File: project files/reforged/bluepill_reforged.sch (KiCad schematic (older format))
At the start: 41 parts, among them J1 USB_C_Receptacle_USB2.0, J2 Left Castellation, J3 STDC14, J4 Right Castellation, J5 STDC14, SW1 Boot0, SW2 Reset, U1 AMS1117-3.3, U2 STM32F103C8Tx, Y1 8MHz, Y2 MC-306, 32768Hz

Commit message: Updates after re-opening in KiCAD 5.1.7
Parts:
- J1: symbol Connector:USB_C_Receptacle_USB2.0 -> bluepill_reforged-rescue:USB_C_Receptacle_USB2.0-Connector
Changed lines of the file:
@@
 Other effective low-drop linear regulators are:\nTI LM3940, up to 1A, but isincompatible in pinout\nLMS8117AMP3.3\n
 $Comp
-L Connector:USB_C_Receptacle_USB2.0 J1
+L bluepill_reforged-rescue:USB_C_Receptacle_USB2.0-Connector J1
 U 1 1 5E12D596
 P 1000 1650

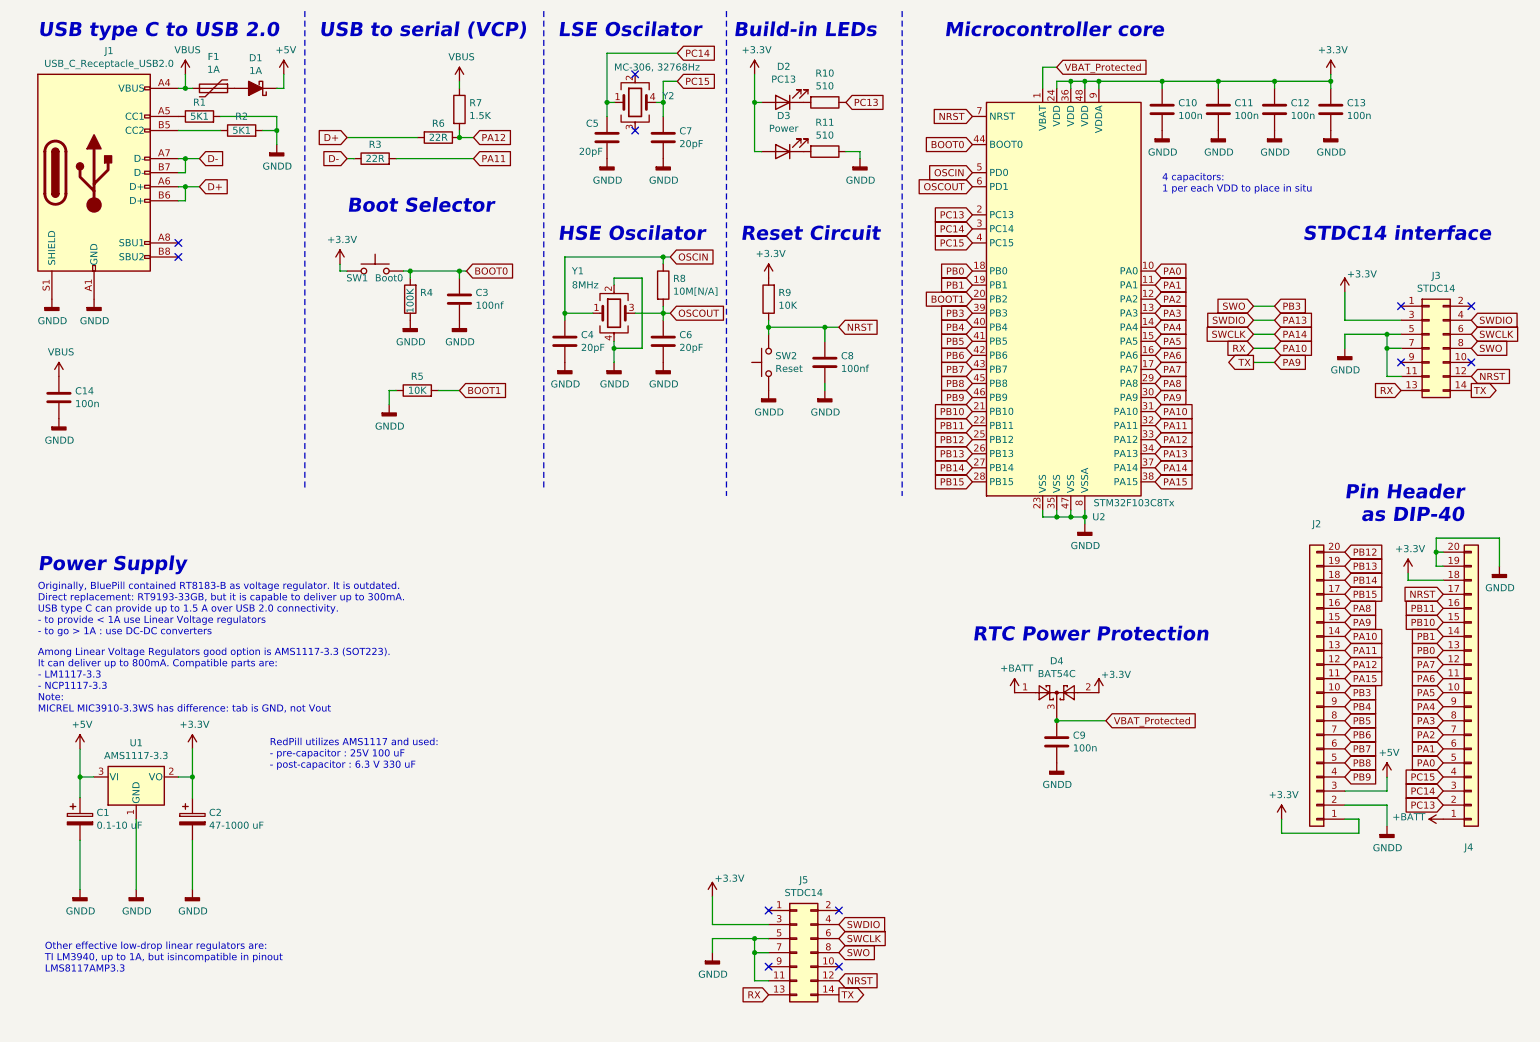
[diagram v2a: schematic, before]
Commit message: Replaced the symbol of STDC14
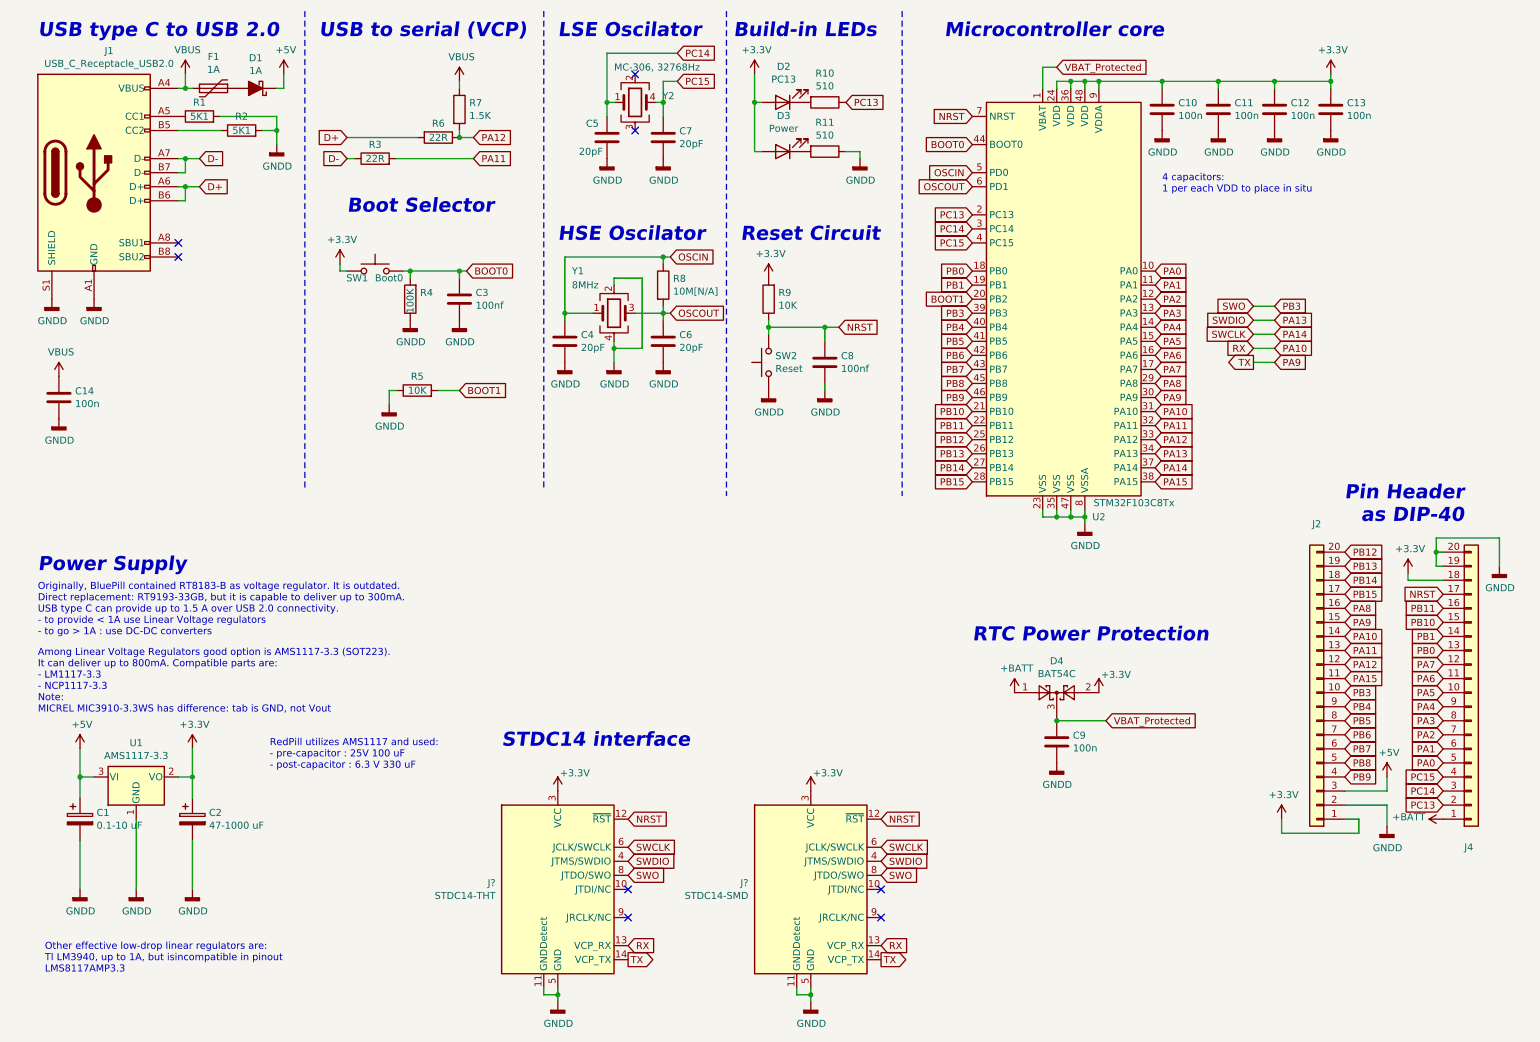
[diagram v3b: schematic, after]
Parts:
- removed J3: STDC14, Connector_PinHeader_1.27mm:PinHeader_2x07_P1.27mm_Vertical_SMD, symbol Connector_Generic:Conn_02x07_Odd_Even
- removed J5: STDC14, Connector_PinHeader_1.27mm:PinHeader_2x07_P1.27mm_Vertical, symbol Connector_Generic:Conn_02x07_Odd_Even
- added J?: STDC14-SMD, symbol Connector:Conn_ST_STDC14
- added J?: STDC14-THT, symbol Connector:Conn_ST_STDC14
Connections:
- net +3V3: now also J?.3 (VCC), J?.3 (VCC)
- net GNDD: now also J?.11 (GNDDetect), J?.11 (GNDDetect), J?.5 (GND), J?.5 (GND), J?.7 (GND), J?.7 (GND)
- net NRST: now also J?.12 (~RST), J?.12 (~RST)
- net PA10: now also J?.13 (VCP_RX), J?.13 (VCP_RX)
- net PA13: now also J?.4 (JTMS/SWDIO), J?.4 (JTMS/SWDIO)
- net PA14: now also J?.6 (JCLK/SWCLK), J?.6 (JCLK/SWCLK)
- net PA9: now also J?.14 (VCP_TX), J?.14 (VCP_TX)
- net PB3: now also J?.8 (JTDO/SWO), J?.8 (JTDO/SWO)
- no-connect marks 12 -> 8
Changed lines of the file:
@@
 Text GLabel 9400 2600 2    50   Input ~ 0
 PB3
-Text Notes 9600 2150 0    100  Italic 20
+Text Notes 3900 5750 0    100  Italic 20
 STDC14 interface
 $Comp
@@
 $EndComp
 Connection ~ 7850 5550
-$Comp
-L Connector_Generic:Conn_02x07_Odd_Even J3
-U 1 1 5E19328C
-P 10500 2900
-F 0 "J3" H 10550 3417 50  0000 C CNN
-F 1 "STDC14" H 10550 3326 50  0000 C CNN
-F 2 "Connector_PinHeader_1.27mm:PinHeader_2x07_P1.27mm_Vertical_SMD" H 10500 2900 50  0001 C CNN
-F 3 "~" H 10500 2900 50  0001 C CNN
-	1    10500 2900
-	1    0    0    -1
-$EndComp
-NoConn ~ 10300 2600
-NoConn ~ 10800 2600
-Text GLabel 10800 2800 2    50   Input ~ 0
-SWCLK
-Text GLabel 10800 3100 2    50   Input ~ 0
-NRST
-Text GLabel 10800 2700 2    50   Input ~ 0
-SWDIO
-$Comp
-L power:+3.3V #PWR037
-U 1 1 5E1A21E5
-P 9900 2500
-F 0 "#PWR037" H 9900 2350 50  0001 C CNN
-F 1 "+3.3V" H 9915 2628 50  0000 L CNN
-F 2 "" H 9900 2500 50  0001 C CNN
-F 3 "" H 9900 2500 50  0001 C CNN
-	1    9900 2500
-	1    0    0    -1
-$EndComp
-Wire Wire Line
-	10300 2700 9900 2700
-Wire Wire Line
-	9900 2700 9900 2500
-Text GLabel 10800 2900 2    50   Input ~ 0
-SWO
-NoConn ~ 10800 3000
-NoConn ~ 10300 3000
-Wire Wire Line
-	10300 2800 10200 2800
-Wire Wire Line
-	10200 2800 10200 2900
-Wire Wire Line
-	10200 2900 10300 2900
-Wire Wire Line
-	10300 3100 10200 3100
-Wire Wire Line
-	10200 3100 10200 2900
-Connection ~ 10200 2900
-Wire Wire Line
-	10200 2800 9900 2800
-Wire Wire Line
-	9900 2800 9900 2900
-Connection ~ 10200 2800
-Text GLabel 10800 3200 2    50   Output ~ 0
-TX
-Text GLabel 10300 3200 0    50   Input ~ 0
-RX
 Text GLabel 9250 2900 0    50   Input ~ 0
 RX
@@
 $EndComp
 $Comp
-L power:GNDD #PWR0117
-U 1 1 5E9096B4
-P 9900 2900
-F 0 "#PWR0117" H 9900 2650 50  0001 C CNN
-F 1 "GNDD" H 9904 2745 50  0000 C CNN
-F 2 "" H 9900 2900 50  0001 C CNN
-F 3 "" H 9900 2900 50  0001 C CNN
-	1    9900 2900
-	1    0    0    -1
-$EndComp
-$Comp
 L power:GNDD #PWR0118
 U 1 1 5E909F75
@@
 Wire Wire Line
 	10200 6150 10200 6300
-$Comp
-L Connector_Generic:Conn_02x07_Odd_Even J5
-U 1 1 5F2A0D58
-P 6000 7200
-F 0 "J5" H 6050 7717 50  0000 C CNN
-F 1 "STDC14" H 6050 7626 50  0000 C CNN
-F 2 "Connector_PinHeader_1.27mm:PinHeader_2x07_P1.27mm_Vertical" H 6000 7200 50  0001 C CNN
-F 3 "~" H 6000 7200 50  0001 C CNN
-	1    6000 7200
-	1    0    0    -1
-$EndComp
-NoConn ~ 5800 6900
-NoConn ~ 6300 6900
-Text GLabel 6300 7100 2    50   Input ~ 0
+Text GLabel 6600 6450 2    50   Input ~ 0
 SWCLK
-Text GLabel 6300 7400 2    50   Input ~ 0
+Text GLabel 6600 6250 2    50   Input ~ 0
 NRST
-Text GLabel 6300 7000 2    50   Input ~ 0
+Text GLabel 6600 6550 2    50   Input ~ 0
 SWDIO
-$Comp
-L power:+3.3V #PWR0110
-U 1 1 5F2A0D63
-P 5400 6800
-F 0 "#PWR0110" H 5400 6650 50  0001 C CNN
-F 1 "+3.3V" H 5415 6928 50  0000 L CNN
-F 2 "" H 5400 6800 50  0001 C CNN
-F 3 "" H 5400 6800 50  0001 C CNN
-	1    5400 6800
-	1    0    0    -1
-$EndComp
-Wire Wire Line
-	5800 7000 5400 7000
-Wire Wire Line
-	5400 7000 5400 6800
-Text GLabel 6300 7200 2    50   Input ~ 0
+Text GLabel 6600 6650 2    50   Input ~ 0
 SWO
-NoConn ~ 6300 7300
-NoConn ~ 5800 7300
-Wire Wire Line
-	5800 7100 5700 7100
-Wire Wire Line
-	5700 7100 5700 7200
-Wire Wire Line
-	5700 7200 5800 7200
-Wire Wire Line
-	5800 7400 5700 7400
-Wire Wire Line
-	5700 7400 5700 7200
-Connection ~ 5700 7200
-Wire Wire Line
-	5700 7100 5400 7100
-Wire Wire Line
-	5400 7100 5400 7200
-Connection ~ 5700 7100
-Text GLabel 6300 7500 2    50   Output ~ 0
+Text GLabel 6600 7250 2    50   Output ~ 0
 TX
-Text GLabel 5800 7500 0    50   Input ~ 0
+Text GLabel 6600 7150 2    50   Input ~ 0
 RX
-$Comp
-L power:GNDD #PWR0129
-U 1 1 5F2A0D79
-P 5400 7200
-F 0 "#PWR0129" H 5400 6950 50  0001 C CNN
-F 1 "GNDD" H 5404 7045 50  0000 C CNN
-F 2 "" H 5400 7200 50  0001 C CNN
-F 3 "" H 5400 7200 50  0001 C CNN
-	1    5400 7200
-	1    0    0    -1
-$EndComp
 $Comp
 L Device:Crystal_GND24 Y1
@@
 	0    -1   -1   0
 $EndComp
+$Comp
+L Connector:Conn_ST_STDC14 J?
+U 1 1 5F95D9CB
+P 6100 6750
+F 0 "J?" H 5656 6796 50  0000 R CNN
+F 1 "STDC14-SMD" H 5656 6705 50  0000 R CNN
+F 2 "" H 6100 6750 50  0001 C CNN
+F 3 "https://www.st.com/content/ccc/resource/technical/document/user_manual/group1/99/49/91/b6/b2/3a/46/e5/DM00526767/files/DM00526767.pdf/jcr:content/translations/en.DM00526767.pdf" V 5750 5500 50  0001 C CNN
+	1    6100 6750
+	1    0    0    -1
+$EndComp
+Wire Wire Line
+	6100 7450 6100 7500
+Wire Wire Line
+	6100 7500 6000 7500
+Wire Wire Line
+	6000 7500 6000 7450
+Wire Wire Line
+	6100 7500 6100 7550
+Connection ~ 6100 7500
+$Comp
+L power:+3.3V #PWR?
+U 1 1 5F96AFF5
+P 6100 6050
+F 0 "#PWR?" H 6100 5900 50  0001 C CNN
+F 1 "+3.3V" H 6115 6178 50  0000 L CNN
+F 2 "" H 6100 6050 50  0001 C CNN
+F 3 "" H 6100 6050 50  0001 C CNN
+	1    6100 6050
+	1    0    0    -1
+$EndComp
+$Comp
+L power:GNDD #PWR?
+U 1 1 5F96C2F7
+P 6100 7550
+F 0 "#PWR?" H 6100 7300 50  0001 C CNN
+F 1 "GNDD" H 6104 7395 50  0000 C CNN
+F 2 "" H 6100 7550 50  0001 C CNN
+F 3 "" H 6100 7550 50  0001 C CNN
+	1    6100 7550
+	1    0    0    -1
+$EndComp
+NoConn ~ 6600 6950
+NoConn ~ 6600 6750
+Text GLabel 4800 6450 2    50   Input ~ 0
+SWCLK
+Text GLabel 4800 6250 2    50   Input ~ 0
+NRST
+Text GLabel 4800 6550 2    50   Input ~ 0
+SWDIO
+Text GLabel 4800 6650 2    50   Input ~ 0
+SWO
+Text GLabel 4800 7250 2    50   Output ~ 0
+TX
+Text GLabel 4800 7150 2    50   Input ~ 0
+RX
+$Comp
+L Connector:Conn_ST_STDC14 J?
+U 1 1 5F984CB7
+P 4300 6750
+F 0 "J?" H 3857 6796 50  0000 R CNN
+F 1 "STDC14-THT" H 3857 6705 50  0000 R CNN
+F 2 "" H 4300 6750 50  0001 C CNN
+F 3 "https://www.st.com/content/ccc/resource/technical/document/user_manual/group1/99/49/91/b6/b2/3a/46/e5/DM00526767/files/DM00526767.pdf/jcr:content/translations/en.DM00526767.pdf" V 3950 5500 50  0001 C CNN
+	1    4300 6750
+	1    0    0    -1
+$EndComp
+Wire Wire Line
+	4300 7450 4300 7500
+Wire Wire Line
+	4300 7500 4200 7500
+Wire Wire Line
+	4200 7500 4200 7450
+Wire Wire Line
+	4300 7500 4300 7550
+Connection ~ 4300 7500
+$Comp
+L power:+3.3V #PWR?
+U 1 1 5F984CC2
+P 4300 6050
+F 0 "#PWR?" H 4300 5900 50  0001 C CNN
+F 1 "+3.3V" H 4315 6178 50  0000 L CNN
+F 2 "" H 4300 6050 50  0001 C CNN
+F 3 "" H 4300 6050 50  0001 C CNN
+	1    4300 6050
+	1    0    0    -1
+$EndComp
+$Comp
+L power:GNDD #PWR?
+U 1 1 5F984CC8
+P 4300 7550
+F 0 "#PWR?" H 4300 7300 50  0001 C CNN
+F 1 "GNDD" H 4304 7395 50  0000 C CNN
+F 2 "" H 4300 7550 50  0001 C CNN
+F 3 "" H 4300 7550 50  0001 C CNN
+	1    4300 7550
+	1    0    0    -1
+$EndComp
+NoConn ~ 4800 6950
+NoConn ~ 4800 6750
 $EndSCHEMATC

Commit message: couple comments
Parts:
- J4: renamed from J?; footprint (none) -> Connector_PinHeader_1.27mm:PinHeader_2x07_P1.27mm_Vertical
- J5: renamed from J?; footprint (none) -> Connector_PinHeader_1.27mm:PinHeader_2x07_P1.27mm_Vertical_SMD
- renumbered C10 to C1, C8 to C10, C14 to C11, C9 to C12, C1 to C13, C2 to C14, C11 to C2, C12 to C3, C13 to C4, C7 to C6, C3 to C7, C4 to C8, C6 to C9, J4 to J3, R10 to R1, R9 to R10, R5 to R11, R7 to R2, R1 to R3, R2 to R4, R6 to R5, R11 to R6, R3 to R7, R4 to R9, U2 to U1, U1 to U2, Y2 to Y1, Y1 to Y2
